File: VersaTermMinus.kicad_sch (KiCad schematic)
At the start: 55 parts, among them CN1 HDMI_A, CN2 DE15_Socket, CN3 USB_B_Micro, CN5 USB_B_Micro, CN6 Mini-DIN-6, CN7 TTL Serial, CN8 DE9 Socket, J2 USBDATA, Q1 2N7002, Q2 2N7002, Q3 2N7002, Q4 2N7002AK, Q5 2N7002, Q6 2N7002, Q7 2N7002, SW1 RESET, SW2 DEFAULTS, SW3 3V3/5V, U1 Raspberry Pi Pico, U3 MAX3232

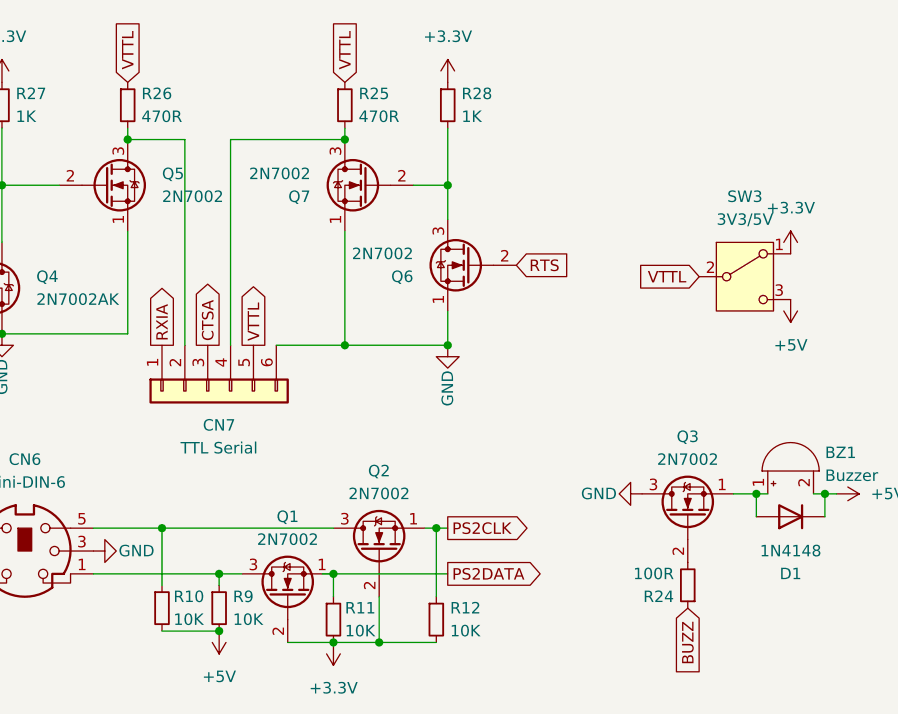
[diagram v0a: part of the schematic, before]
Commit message: record digikey part numbers
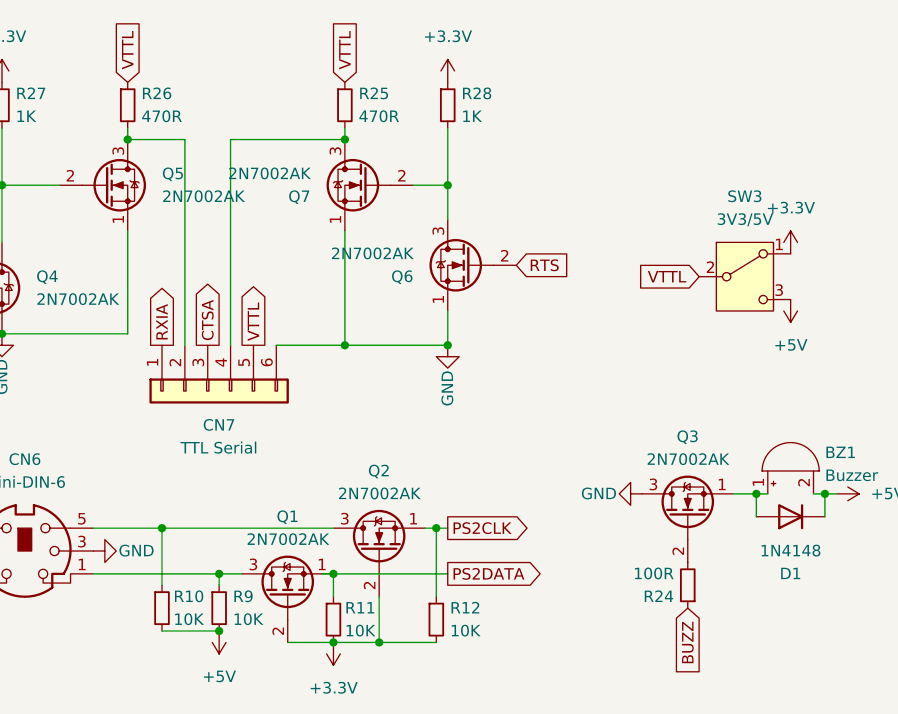
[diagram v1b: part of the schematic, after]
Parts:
- CN1: DigiKey (none) -> 609-4614-1-ND
- CN2: DigiKey (none) -> L77HDE15SD1CH4FVGA-ND
- CN3, CN5: DigiKey (none) -> 732-5960-1-ND
- CN8: DigiKey (none) -> AE10968-ND
- D1, D3, D4, D5, D6: DigiKey (none) -> 1N4148WXTPMSCT-ND
- D2: DigiKey (none) -> 641-1762-1-ND
- Q1, Q2, Q3, Q5, Q6, Q7: value 2N7002 -> 2N7002AK
- RN1: DigiKey (none) -> 4816P-1-271LFCT-ND
- SW1, SW2: DigiKey (none) -> 450-1157-ND
- SW3: DigiKey (none) -> CKN9559-ND
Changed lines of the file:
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@@
 			)
 		)
+		(property "DigiKey" "4816P-1-271LFCT-ND"
+			(at 71.12 45.72 0)
+			(effects
+				(font
+					(size 1.27 1.27)
+				)
+				(hide yes)
+			)
+		)
 		(pin "10"
 		)
@@
 			)
 		)
+		(property "DigiKey" "1N4148WXTPMSCT-ND"
+			(at 43.18 104.14 0)
+			(effects
+				(font
+					(size 1.27 1.27)
+				)
+				(hide yes)
+			)
+		)
 		(pin "2"
 		)
@@
 			)
 		)
+		(property "DigiKey" "609-4614-1-ND"
+			(at 83.82 30.48 90)
+			(effects
+				(font
+					(size 1.27 1.27)
+				)
+				(hide yes)
+			)
+		)
 		(pin "3"
 		)
@@
 			)
 		)
+		(property "DigiKey" "732-5960-1-ND"
+			(at 26.67 63.5 0)
+			(effects
+				(font
+					(size 1.27 1.27)
+				)
+				(hide yes)
+			)
+		)
 		(pin "3"
 		)
@@
 			)
 		)
+		(property "DigiKey" "1N4148WXTPMSCT-ND"
+			(at 43.18 83.82 0)
+			(effects
+				(font
+					(size 1.27 1.27)
+				)
+				(hide yes)
+			)
+		)
 		(pin "2"
 		)
@@
 			)
 		)
+		(property "DigiKey" "4816P-1-271LFCT-ND"
+			(at 73.66 45.72 0)
+			(effects
+				(font
+					(size 1.27 1.27)
+				)
+				(hide yes)
+			)
+		)
 		(pin "10"
 		)
@@
 			)
 		)
-		(property "Value" "2N7002"
+		(property "Value" "2N7002AK"
 			(at 59.69 179.07 90)
 			(effects
@@
 			)
 		)
+		(property "DigiKey" "450-1157-ND"
+			(at 161.29 21.59 0)
+			(effects
+				(font
+					(size 1.27 1.27)
+				)
+				(hide yes)
+			)
+		)
 		(pin "2"
 		)
@@
 			)
 		)
-		(property "Value" "2N7002"
+		(property "Value" "2N7002AK"
 			(at 45.72 140.9699 0)
 			(effects
@@
 			)
 		)
+		(property "DigiKey" "4816P-1-271LFCT-ND"
+			(at 66.04 45.72 0)
+			(effects
+				(font
+					(size 1.27 1.27)
+				)
+				(hide yes)
+			)
+		)
 		(pin "10"
 		)
@@
 			)
 		)
+		(property "DigiKey" "4816P-1-271LFCT-ND"
+			(at 68.58 45.72 0)
+			(effects
+				(font
+					(size 1.27 1.27)
+				)
+				(hide yes)
+			)
+		)
 		(pin "10"
 		)
@@
 			)
 		)
-		(property "Value" "2N7002"
+		(property "Value" "2N7002AK"
 			(at 69.85 173.99 90)
 			(effects
@@
 			)
 		)
+		(property "DigiKey" "4816P-1-271LFCT-ND"
+			(at 76.2 45.72 0)
+			(effects
+				(font
+					(size 1.27 1.27)
+				)
+				(hide yes)
+			)
+		)
 		(pin "10"
 		)
@@
 			)
 		)
+		(property "DigiKey" "641-1762-1-ND"
+			(at 39.37 24.13 0)
+			(effects
+				(font
+					(size 1.27 1.27)
+				)
+				(hide yes)
+			)
+		)
 		(pin "1"
 		)
@@
 			)
 		)
+		(property "DigiKey" "1N4148WXTPMSCT-ND"
+			(at 43.18 109.22 0)
+			(effects
+				(font
+					(size 1.27 1.27)
+				)
+				(hide yes)
+			)
+		)
 		(pin "2"
 		)
@@
 			)
 		)
+		(property "DigiKey" "4816P-1-271LFCT-ND"
+			(at 63.5 45.72 0)
+			(effects
+				(font
+					(size 1.27 1.27)
+				)
+				(hide yes)
+			)
+		)
 		(pin "10"
 		)
@@
 			)
 		)
+		(property "DigiKey" "AE10968-ND"
+			(at 266.7 138.43 0)
+			(effects
+				(font
+					(size 1.27 1.27)
+				)
+				(hide yes)
+			)
+		)
 		(pin "6"
 		)
@@
 			)
 		)
+		(property "DigiKey" "1N4148WXTPMSCT-ND"
+			(at 43.18 88.9 0)
+			(effects
+				(font
+					(size 1.27 1.27)
+				)
+				(hide yes)
+			)
+		)
 		(pin "2"
 		)
@@
 			)
 		)
-		(property "Value" "2N7002"
+		(property "Value" "2N7002AK"
 			(at 73.66 147.3201 0)
 			(effects
@@
 			)
 		)
+		(property "DigiKey" "1N4148WXTPMSCT-ND"
+			(at 115.57 176.53 0)
+			(effects
+				(font
+					(size 1.27 1.27)
+				)
+				(hide yes)
+			)
+		)
 		(pin "2"
 		)
@@
 			)
 		)
+		(property "DigiKey" "L77HDE15SD1CH4FVGA-ND"
+			(at 259.08 38.1 0)
+			(effects
+				(font
+					(size 1.27 1.27)
+				)
+				(hide yes)
+			)
+		)
 		(pin "13"
 		)
@@
 			)
 		)
+		(property "DigiKey" "4816P-1-271LFCT-ND"
+			(at 78.74 45.72 0)
+			(effects
+				(font
+					(size 1.27 1.27)
+				)
+				(hide yes)
+			)
+		)
 		(pin "10"
 		)
@@
 			)
 		)
+		(property "DigiKey" "CKN9559-ND"
+			(at 110.49 149.86 0)
+			(effects
+				(font
+					(size 1.27 1.27)
+				)
+				(hide yes)
+			)
+		)
 		(pin "3"
 		)
@@
 			)
 		)
+		(property "DigiKey" "4816P-1-271LFCT-ND"
+			(at 81.28 45.72 0)
+			(effects
+				(font
+					(size 1.27 1.27)
+				)
+				(hide yes)
+			)
+		)
 		(pin "10"
 		)
@@
 			)
 		)
-		(property "Value" "2N7002"
+		(property "Value" "2N7002AK"
 			(at 104.14 170.18 90)
 			(effects
@@
 			)
 		)
-		(property "Value" "2N7002"
+		(property "Value" "2N7002AK"
 			(at 62.23 138.4301 0)
 			(effects
@@
 			)
 		)
+		(property "DigiKey" "732-5960-1-ND"
+			(at 26.67 29.21 0)
+			(effects
+				(font
+					(size 1.27 1.27)
+				)
+				(hide yes)
+			)
+		)
 		(pin "3"
 		)
@@
 			(at 198.12 21.59 0)
 			(effects
+				(font
+					(size 1.27 1.27)
+				)
+				(hide yes)
+			)
+		)
+		(property "DigiKey" "450-1157-ND"
+			(at 198.12 21.59 0)
+			(effects

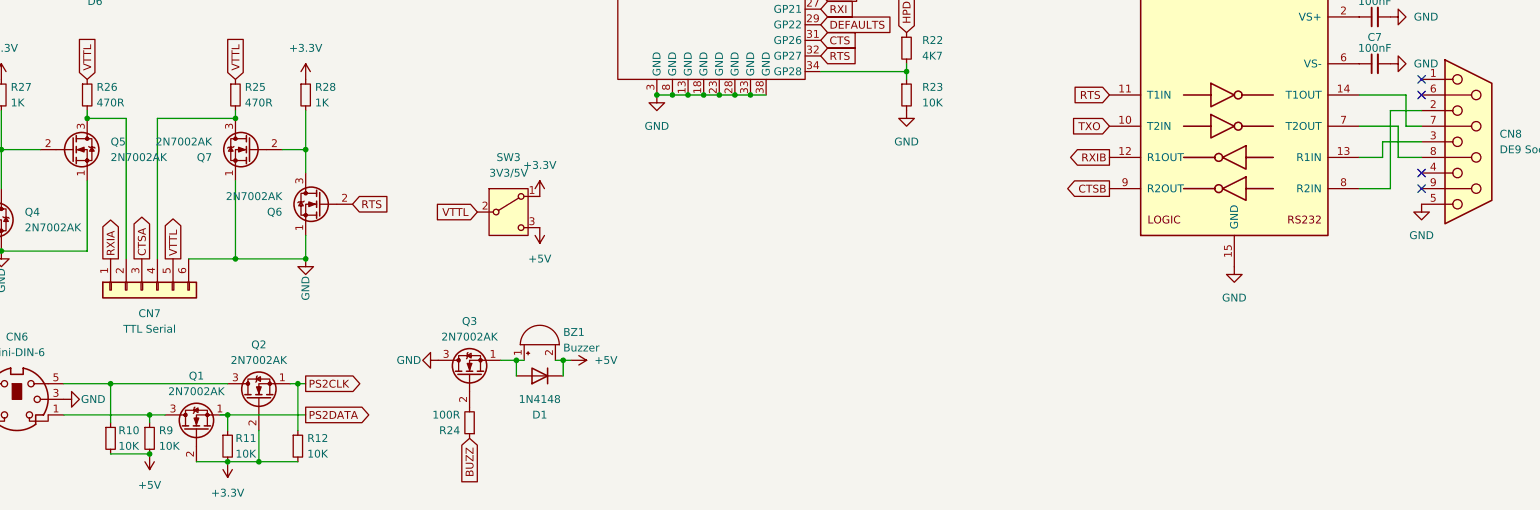
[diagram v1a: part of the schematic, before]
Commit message: fix de9 and buzzer
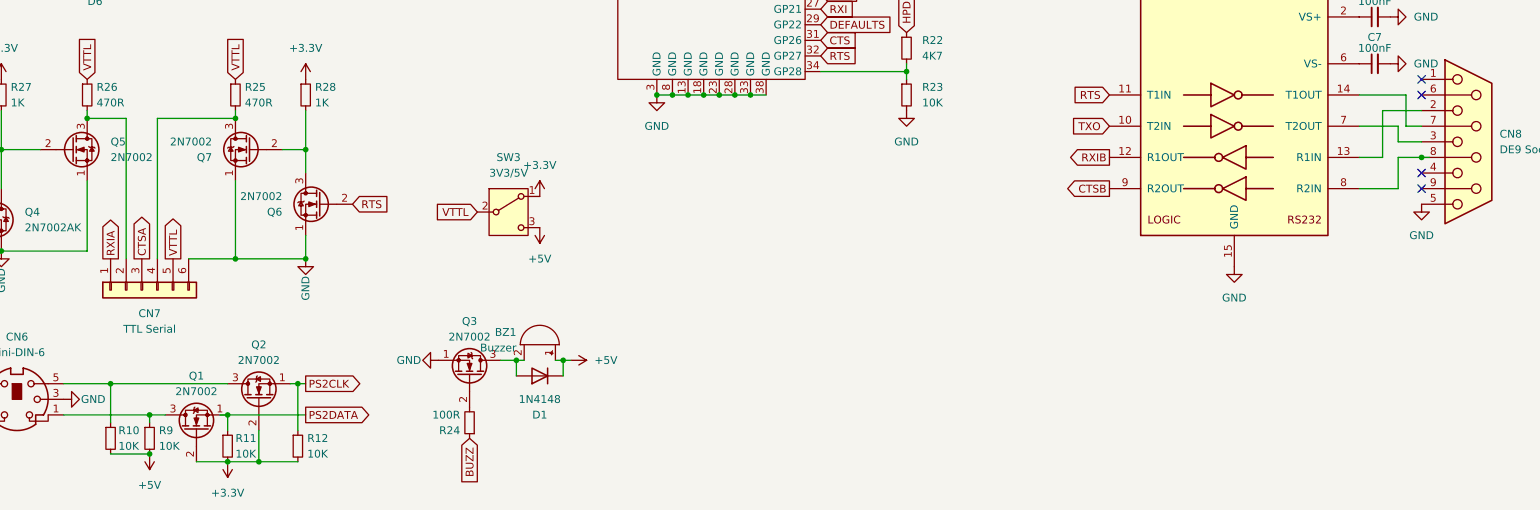
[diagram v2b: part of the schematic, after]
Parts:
- CN1: DigiKey 609-4614-1-ND -> (none)
- CN2: DigiKey L77HDE15SD1CH4FVGA-ND -> (none)
- CN3, CN5: DigiKey 732-5960-1-ND -> (none)
- CN8: DigiKey AE10968-ND -> (none)
- D1, D3, D4, D5, D6: DigiKey 1N4148WXTPMSCT-ND -> (none)
- D2: DigiKey 641-1762-1-ND -> (none)
- Q1, Q2, Q3, Q5, Q6, Q7: value 2N7002AK -> 2N7002
- RN1: DigiKey 4816P-1-271LFCT-ND -> (none)
- SW1, SW2: DigiKey 450-1157-ND -> (none)
- SW3: DigiKey CKN9559-ND -> (none)
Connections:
- net +5V: now also BZ1.1 (+); no longer BZ1.2 (-)
- net GND: now also Q3.1 (S); no longer Q3.3 (D)
- net at CN8.2: now also U3.13 (R1IN); no longer U3.8 (R2IN)
- net at CN8.3: now also U3.7 (T2OUT); no longer U3.13 (R1IN)
- net at CN8.8: now also U3.8 (R2IN); no longer U3.7 (T2OUT)
- new net: BZ1.2 (-), D1.2 (A), Q3.3 (D)
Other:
- moved on the sheet: BZ1, Q3

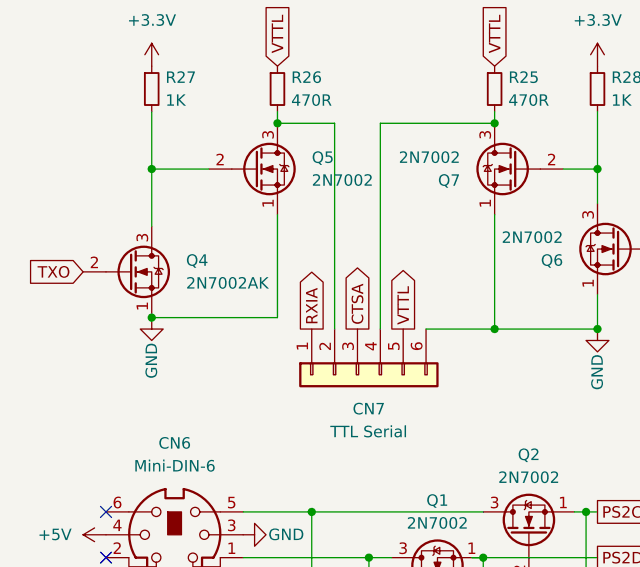
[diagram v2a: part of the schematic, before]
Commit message: populate missing BOM fields
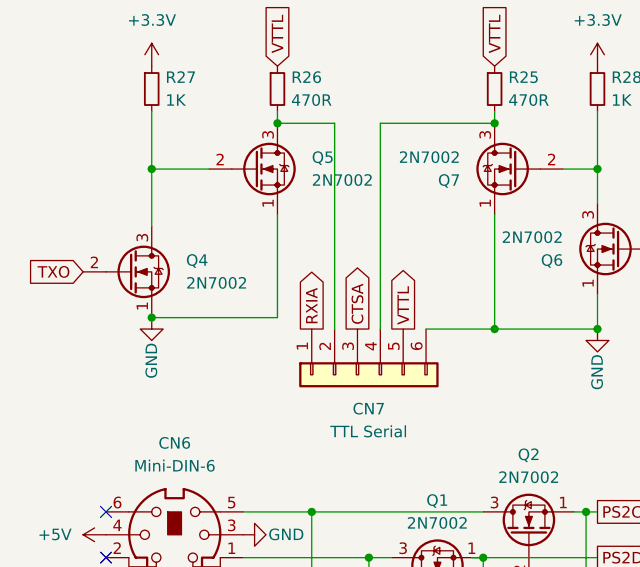
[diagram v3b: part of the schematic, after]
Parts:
- CN1: DigiKey (none) -> 609-4614-1-ND
- CN2: DigiKey (none) -> L77HDE15SD1CH4FVGA-ND
- CN3, CN5: DigiKey (none) -> 732-5960-1-ND
- CN8: DigiKey (none) -> AE10968-ND
- D1, D3, D4, D5, D6: DigiKey (none) -> 1N4148WXTPMSCT-ND
- D2: DigiKey (none) -> 641-1762-1-ND
- Q4: value 2N7002AK -> 2N7002
- RN1: DigiKey (none) -> 4816P-1-271LFCT-ND
- SW1, SW2: DigiKey (none) -> CKN10734-ND
- SW3: DigiKey (none) -> CKN9559-ND
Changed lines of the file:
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@@
 			)
 		)
-		(property "Datasheet" "~"
+		(property "Datasheet" "https://www.bourns.com/docs/Product-Datasheets/4800P.pdf"
 			(at 71.12 45.72 0)
 			(effects
@@
 			)
 		)
+		(property "DigiKey" "4816P-1-271LFCT-ND"
+			(at 71.12 45.72 0)
+			(effects
+				(font
+					(size 1.27 1.27)
+				)
+				(hide yes)
+			)
+		)
 		(pin "10"
 		)
@@
 			)
 		)
+		(property "DigiKey" "1N4148WXTPMSCT-ND"
+			(at 43.18 104.14 0)
+			(effects
+				(font
+					(size 1.27 1.27)
+				)
+				(hide yes)
+			)
+		)
 		(pin "2"
 		)
@@
 			)
 		)
+		(property "DigiKey" "609-4614-1-ND"
+			(at 83.82 30.48 90)
+			(effects
+				(font
+					(size 1.27 1.27)
+				)
+				(hide yes)
+			)
+		)
 		(pin "3"
 		)
@@
 			)
 		)
-		(property "Datasheet" "~"
+		(property "Datasheet" "https://www.we-online.com/katalog/datasheet/629105150521.pdf"
 			(at 30.48 64.77 0)
 			(effects
@@
 			)
 		)
+		(property "DigiKey" "732-5960-1-ND"
+			(at 26.67 63.5 0)
+			(effects
+				(font
+					(size 1.27 1.27)
+				)
+				(hide yes)
+			)
+		)
 		(pin "3"
 		)
@@
 			)
 		)
+		(property "DigiKey" "1N4148WXTPMSCT-ND"
+			(at 43.18 83.82 0)
+			(effects
+				(font
+					(size 1.27 1.27)
+				)
+				(hide yes)
+			)
+		)
 		(pin "2"
 		)
@@
 			)
 		)
-		(property "Datasheet" "~"
+		(property "Datasheet" "https://www.bourns.com/docs/Product-Datasheets/4800P.pdf"
 			(at 73.66 45.72 0)
 			(effects
@@
 			)
 		)
+		(property "DigiKey" "4816P-1-271LFCT-ND"
+			(at 73.66 45.72 0)
+			(effects
+				(font
+					(size 1.27 1.27)
+				)
+				(hide yes)
+			)
+		)
 		(pin "10"
 		)
@@
 			)
 		)
-		(property "Datasheet" "~"
+		(property "Datasheet" "https://www.ckswitches.com/media/1457/ksa_ksl.pdf"
 			(at 161.29 16.51 0)
 			(effects
@@
 			)
 		)
+		(property "DigiKey" "CKN10734-ND"
+			(at 161.29 21.59 0)
+			(effects
+				(font
+					(size 1.27 1.27)
+				)
+				(hide yes)
+			)
+		)
 		(pin "2"
 		)
@@
 			)
 		)
-		(property "Datasheet" "~"
+		(property "Datasheet" "https://www.bourns.com/docs/Product-Datasheets/4800P.pdf"
 			(at 66.04 45.72 0)
 			(effects
@@
 			)
 		)
+		(property "DigiKey" "4816P-1-271LFCT-ND"
+			(at 66.04 45.72 0)
+			(effects
+				(font
+					(size 1.27 1.27)
+				)
+				(hide yes)
+			)
+		)
 		(pin "10"
 		)
@@
 			)
 		)
-		(property "Datasheet" "~"
+		(property "Datasheet" "https://www.bourns.com/docs/Product-Datasheets/4800P.pdf"
 			(at 68.58 45.72 0)
 			(effects
@@
 			)
 		)
+		(property "DigiKey" "4816P-1-271LFCT-ND"
+			(at 68.58 45.72 0)
+			(effects
+				(font
+					(size 1.27 1.27)
+				)
+				(hide yes)
+			)
+		)
 		(pin "10"
 		)
@@
 			)
 		)
-		(property "Datasheet" "~"
+		(property "Datasheet" "https://www.bourns.com/docs/Product-Datasheets/4800P.pdf"
 			(at 76.2 45.72 0)
 			(effects
@@
 			)
 		)
+		(property "DigiKey" "4816P-1-271LFCT-ND"
+			(at 76.2 45.72 0)
+			(effects
+				(font
+					(size 1.27 1.27)
+				)
+				(hide yes)
+			)
+		)
 		(pin "10"
 		)
@@
 			)
 		)
+		(property "DigiKey" "641-1762-1-ND"
+			(at 39.37 24.13 0)
+			(effects
+				(font
+					(size 1.27 1.27)
+				)
+				(hide yes)
+			)
+		)
 		(pin "1"
 		)
@@
 			)
 		)
-		(property "Value" "2N7002AK"
+		(property "Value" "2N7002"
 			(at 31.75 152.3999 0)
 			(effects
@@
 			)
 		)
+		(property "DigiKey" "1N4148WXTPMSCT-ND"
+			(at 43.18 109.22 0)
+			(effects
+				(font
+					(size 1.27 1.27)
+				)
+				(hide yes)
+			)
+		)
 		(pin "2"
 		)
@@
 			)
 		)
-		(property "Datasheet" "~"
+		(property "Datasheet" "https://www.bourns.com/docs/Product-Datasheets/4800P.pdf"
 			(at 63.5 45.72 0)
 			(effects
@@
 			)
 		)
+		(property "DigiKey" "4816P-1-271LFCT-ND"
+			(at 63.5 45.72 0)
+			(effects
+				(font
+					(size 1.27 1.27)
+				)
+				(hide yes)
+			)
+		)
 		(pin "10"
 		)
@@
 			)
 		)
+		(property "DigiKey" "AE10968-ND"
+			(at 266.7 138.43 0)
+			(effects
+				(font
+					(size 1.27 1.27)
+				)
+				(hide yes)
+			)
+		)
 		(pin "6"
 		)
@@
 			)
 		)
+		(property "DigiKey" "1N4148WXTPMSCT-ND"
+			(at 43.18 88.9 0)
+			(effects
+				(font
+					(size 1.27 1.27)
+				)
+				(hide yes)
+			)
+		)
 		(pin "2"
 		)
@@
 			)
 		)
+		(property "DigiKey" "1N4148WXTPMSCT-ND"
+			(at 115.57 176.53 0)
+			(effects
+				(font
+					(size 1.27 1.27)
+				)
+				(hide yes)
+			)
+		)
 		(pin "2"
 		)
@@
 			)
 		)
+		(property "DigiKey" "L77HDE15SD1CH4FVGA-ND"
+			(at 259.08 38.1 0)
+			(effects
+				(font
+					(size 1.27 1.27)
+				)
+				(hide yes)
+			)
+		)
 		(pin "13"
 		)
@@
 			)
 		)
-		(property "Datasheet" "~"
+		(property "Datasheet" "https://www.bourns.com/docs/Product-Datasheets/4800P.pdf"
 			(at 78.74 45.72 0)
 			(effects
@@
 			)
 		)
+		(property "DigiKey" "4816P-1-271LFCT-ND"
+			(at 78.74 45.72 0)
+			(effects
+				(font
+					(size 1.27 1.27)
+				)
+				(hide yes)
+			)
+		)
 		(pin "10"
 		)
@@
 			)
 		)
-		(property "Datasheet" "~"
+		(property "Datasheet" "https://www.ckswitches.com/media/1428/os.pdf"
 			(at 110.49 157.48 0)
 			(effects
@@
 			)
 		)
+		(property "DigiKey" "CKN9559-ND"
+			(at 110.49 149.86 0)
+			(effects
+				(font
+					(size 1.27 1.27)
+				)
+				(hide yes)
+			)
+		)
 		(pin "3"
 		)
@@
 			)
 		)
-		(property "Datasheet" "~"
+		(property "Datasheet" "https://www.bourns.com/docs/Product-Datasheets/4800P.pdf"
 			(at 81.28 45.72 0)
 			(effects
@@
 			)
 		)
+		(property "DigiKey" "4816P-1-271LFCT-ND"
+			(at 81.28 45.72 0)
+			(effects
+				(font
+					(size 1.27 1.27)
+				)
+				(hide yes)
+			)
+		)
 		(pin "10"
 		)
@@
 			)
 		)
-		(property "Datasheet" "~"
+		(property "Datasheet" "https://www.we-online.com/katalog/datasheet/629105150521.pdf"
 			(at 30.48 30.48 0)
 			(effects
@@
 			)
 		)
+		(property "DigiKey" "732-5960-1-ND"
+			(at 26.67 29.21 0)
+			(effects
+				(font
+					(size 1.27 1.27)
+				)
+				(hide yes)
+			)
+		)
 		(pin "3"
 		)
@@
 			)
 		)
-		(property "Datasheet" "~"
+		(property "Datasheet" "https://www.ckswitches.com/media/1457/ksa_ksl.pdf"
 			(at 198.12 16.51 0)
 			(effects
@@
 			(at 198.12 21.59 0)
 			(effects
+				(font
+					(size 1.27 1.27)
+				)
+				(hide yes)
+			)
+		)
+		(property "DigiKey" "CKN10734-ND"
+			(at 198.12 21.59 0)
+			(effects
